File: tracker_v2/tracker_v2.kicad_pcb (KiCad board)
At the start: 2 copper layers, 69 x 51.6 mm, 26 parts, among them J1 USB_C_Receptacle_PowerOnly_6P, Q1 DMG9926UDM-7, U1 XIAO-ESP32-C6-SMD, U2 LIS3DH, U3 DW01A, U4 INA226AIDGSR, U5 TP4056-42-ESOP8

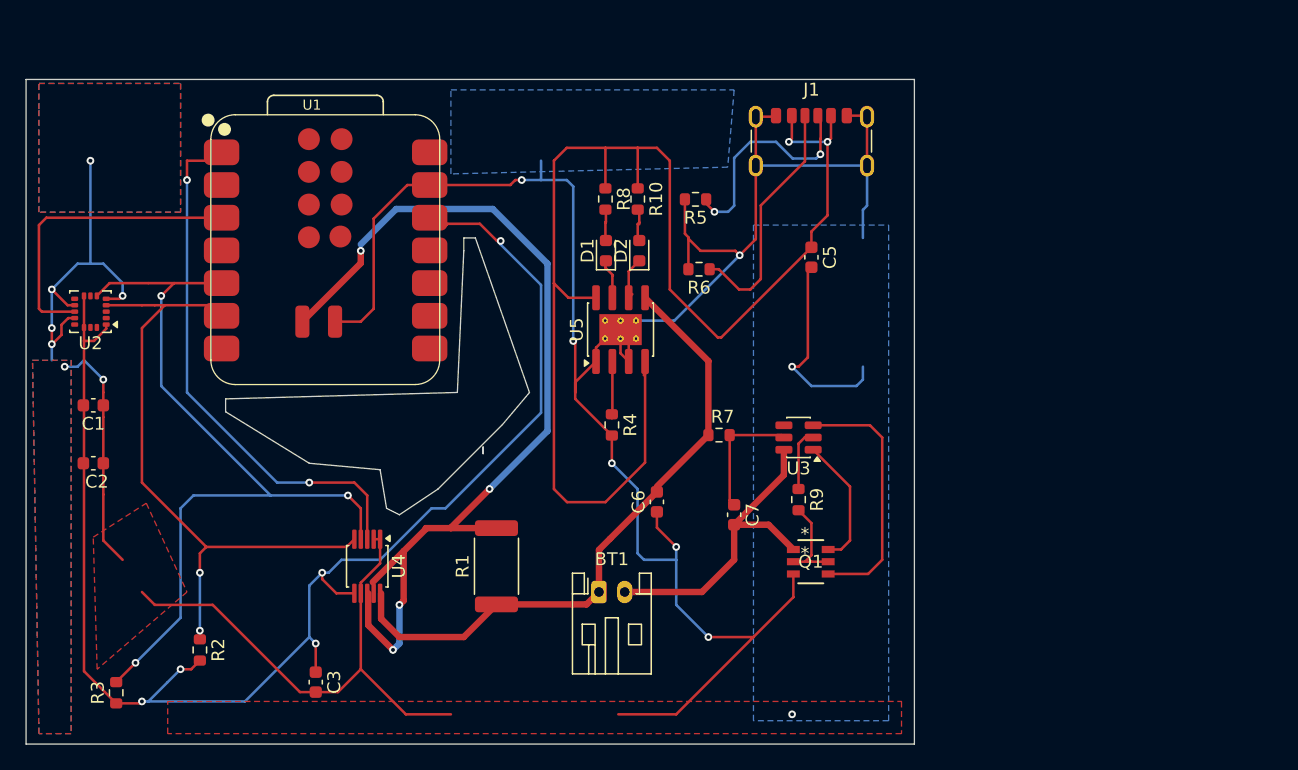
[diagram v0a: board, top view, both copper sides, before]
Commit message: started v2 , placement sure routing is being done
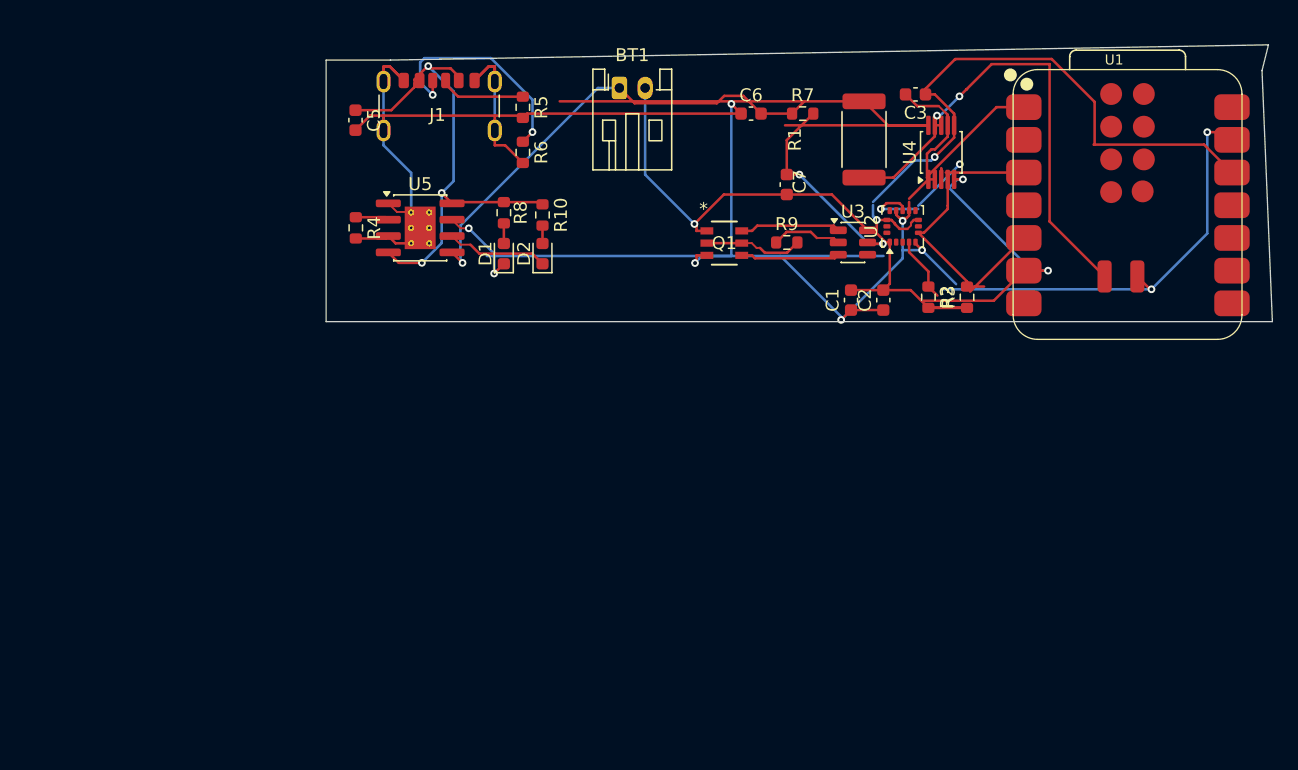
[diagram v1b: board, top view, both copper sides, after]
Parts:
- moved R3 72.9 mm to (170.1, 92.6)
- moved C3 65.2 mm to (166.1, 76.9), turned to 180 degrees
- moved U2 63.4 mm to (165.1, 87.1), turned to 90 degrees
- moved R2 62.9 mm to (167.1, 92.6)
- moved C2 62.7 mm to (163.6, 92.8), turned to 90 degrees
- moved U1 62.4 mm to (173.7, 96.0)
- moved C1 59.4 mm to (161.1, 92.8), turned to 90 degrees
- moved U4 55.0 mm to (168.1, 81.4), turned to 90 degrees
- moved R1 43.7 mm to (162.1, 80.4), turned to -90 degrees
- moved BT1 39.2 mm to (143.1, 76.4)
- moved C5 37.0 mm to (122.6, 78.9)
- moved C6 31.0 mm to (153.3, 78.3), turned to 0 degrees
- moved J1 29.0 mm to (129.1, 78.9)
- moved C7 26.0 mm to (156.1, 83.9)
- moved R7 25.8 mm to (157.3, 78.3)
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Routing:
- net GND: track 272.2 -> 201.3 mm, vias 15 -> 7
- net USB_VBUS: track 104.9 -> 39.2 mm, vias 2 -> 3
- net 3v3: track 112.7 -> 68.0 mm, vias 5 -> 2
- net SDA: track 63.3 -> 18.7 mm, vias 3 -> 0
- net /Shunt_Output: track 73.0 -> 37.7 mm, vias 4 -> 2
- net Net-(U1-D0): track 41.7 -> 10.6 mm, vias 2 -> 0
- net /Charging_and_Battery/BAT+: track 48.9 -> 77.5 mm, vias 0 -> 1
- net SCL: track 50.0 -> 28.1 mm
- net Net-(U3-OC): track 19.9 -> 7.71 mm
- net Net-(J1-CC2): track 17.7 -> 6.68 mm, vias 2 -> 0
- net Net-(U1-D2): track 23.8 -> 15.8 mm, vias 0 -> 2
- net Net-(U3-VCC): track 9.85 -> 16.5 mm, vias 0 -> 2
- net Net-(D2-K): track 3.67 -> 7.92 mm
- net /Charging_and_Battery/BAT-: track 25.1 -> 29.1 mm, vias 0 -> 1
- net Net-(D1-K): track 3.05 -> 6.97 mm, vias 0 -> 2
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- removed copper zone on B.Cu, net GND
- removed copper zone on F.Cu, net GND
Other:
- board size 69 x 51.6 mm -> 73.5 x 21.5 mm

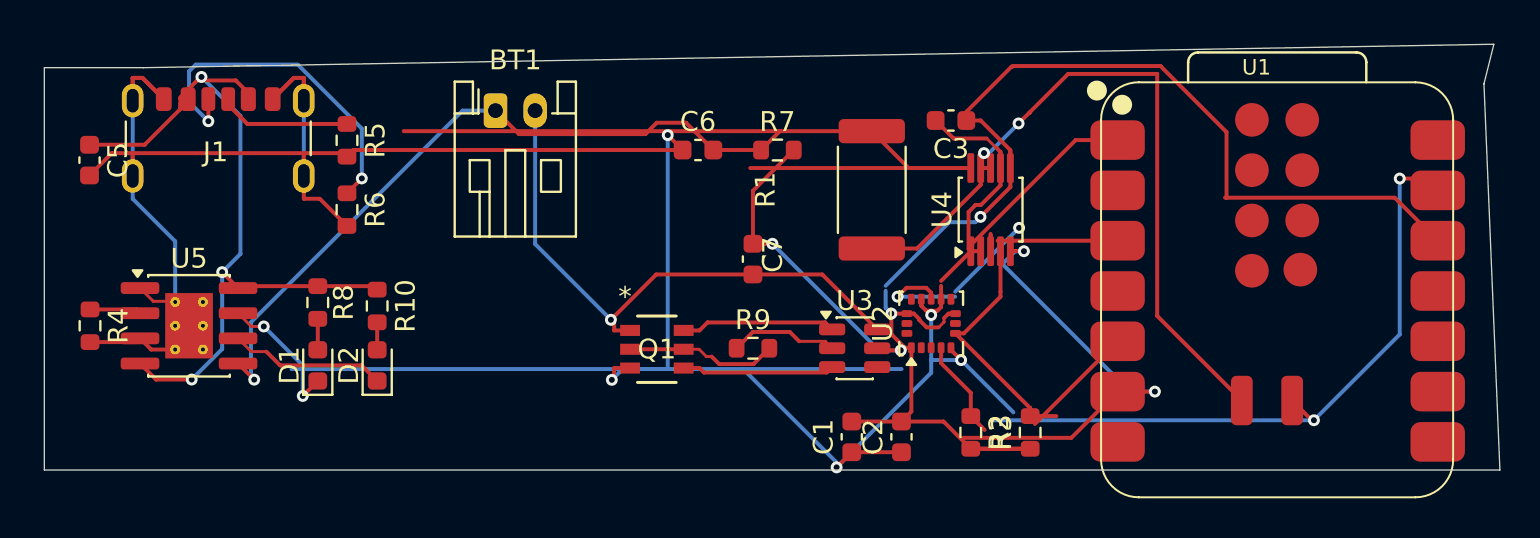
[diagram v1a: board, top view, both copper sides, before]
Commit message: added some connections
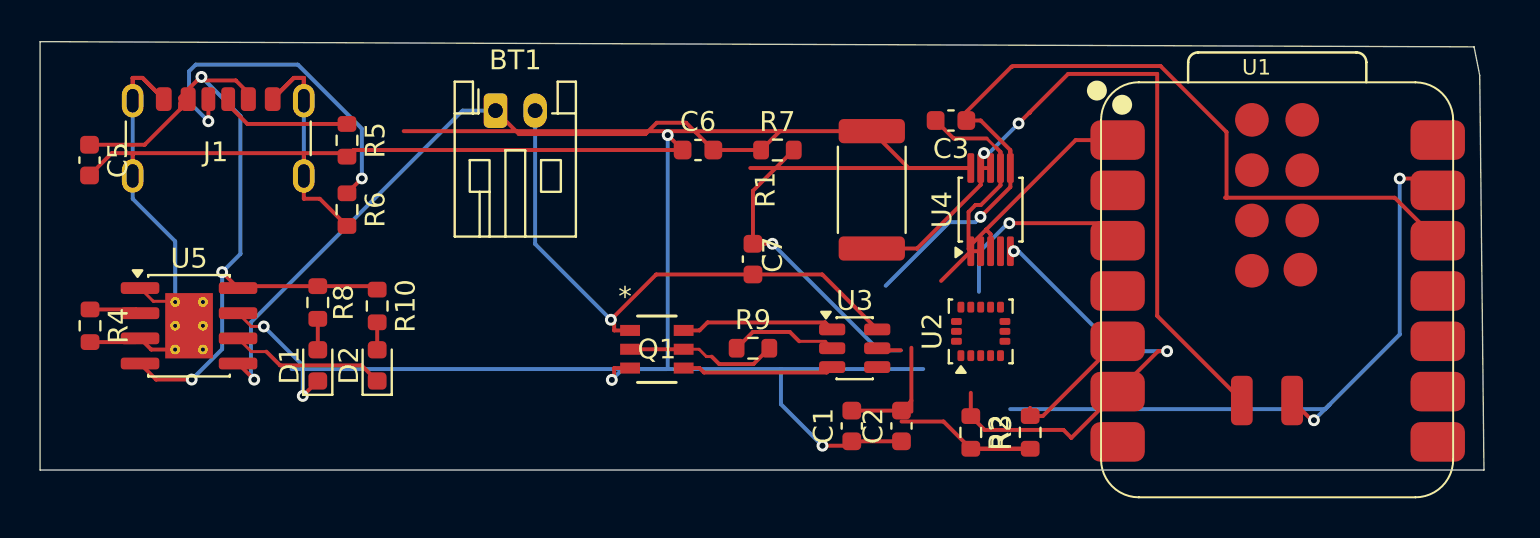
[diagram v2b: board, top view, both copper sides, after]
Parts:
- moved U2 2.53 mm to (167.6, 87.5)
- moved C1 0.55 mm to (161.1, 92.3)
- moved C2 0.55 mm to (163.6, 92.3)
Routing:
- net GND: track 201.3 -> 182.4 mm, vias 7 -> 5
- net SDA: track 18.7 -> 6.78 mm
- net 3v3: track 68.0 -> 60.4 mm, vias 2 -> 1
- net Net-(U1-D2): track 15.8 -> 10.0 mm, vias 2 -> 1
- net SCL: track 28.1 -> 23.2 mm
- net Net-(U3-VCC): vias 2 -> 1
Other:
- board size 73.5 x 21.5 mm -> 72.9 x 21.6 mm

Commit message: completed v2 routing
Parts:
- added TP1: TestPoint, TestPoint:TestPoint_Pad_D1.0mm, F.Cu at (124.5, 92.0)
- added TP2: TestPoint, TestPoint:TestPoint_Pad_D1.0mm, F.Cu at (145.5, 92.5)
- added TP3: TestPoint, TestPoint:TestPoint_Pad_D1.0mm, F.Cu at (171.0, 87.5)
- added TP4: TestPoint, TestPoint:TestPoint_Pad_D1.0mm, F.Cu at (171.5, 85.0)
- added TP5: TestPoint, TestPoint:TestPoint_Pad_D1.0mm, F.Cu at (171.5, 82.0)
- added TP6: TestPoint, TestPoint:TestPoint_Pad_D1.0mm, F.Cu at (170.0, 74.0)
- added TP7: TestPoint, TestPoint:TestPoint_Pad_D1.0mm, F.Cu at (125.0, 74.5)
- added TP8: TestPoint, TestPoint:TestPoint_Pad_D1.0mm, F.Cu at (151.0, 75.5)
- moved J1 2.90 mm to (131.8, 77.8)
- moved R5 2.90 mm to (138.3, 76.8)
- moved R6 2.90 mm to (138.3, 80.3)
- moved R4 2.90 mm to (125.3, 86.2)
- moved C5 2.90 mm to (125.3, 77.8)
- moved U5 2.90 mm to (130.3, 86.2)
- moved D1 2.90 mm to (136.8, 88.2)
- moved D2 2.90 mm to (139.8, 88.2)
- moved R10 2.90 mm to (139.8, 85.2)
- moved R8 2.90 mm to (136.8, 85.0)
- moved R2 0.43 mm to (167.1, 92.2)
- moved R3 0.43 mm to (170.1, 92.2)
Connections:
- U2 pad 7: unconnected-(U2-SDO-Pad7) -> 3v3
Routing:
- net GND: track 182.4 -> 246.9 mm, vias 5 -> 12
- net /Charging_and_Battery/BAT+: track 77.5 -> 45.9 mm, vias 1 -> 2
- net USB_VBUS: track 39.2 -> 51.0 mm
- net 3v3: track 60.4 -> 70.7 mm, vias 1 -> 2
- net SDA: track 6.78 -> 16.2 mm
- net (no net): track 0.00 -> 2.11 mm, vias 0 -> 3
- net Net-(U1-D0): track 10.9 -> 9.51 mm
- net Net-(U3-VCC): track 16.5 -> 15.2 mm, vias 1 -> 2
- net SCL: track 23.2 -> 24.3 mm
- net /Shunt_Output: track 37.7 -> 38.7 mm
- net Net-(U1-D2): track 10.0 -> 10.8 mm, vias 1 -> 2
- net /Charging_and_Battery/BAT-: track 29.1 -> 29.3 mm, vias 1 -> 2
- added copper zone on B.Cu, net GND
- added copper zone on F.Cu, net GND
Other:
- board size 72.9 x 21.6 mm -> 71 x 22.1 mm
- board text added: "+"
- board text added: "-"

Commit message: removed a GND trace under the chip and connected it to a common ground
like the title says
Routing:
- net GND: track 246.9 -> 235.6 mm
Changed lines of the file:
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@@
 	)
 	(segment
-		(start 180.5 88.5)
-		(end 184 88.5)
+		(start 188.747 79.7814)
+		(end 188.5284 80)
 		(width 0.2)
 		(layer "B.Cu")
@@
 	)
 	(segment
-		(start 186.25 86.25)
-		(end 188.747 83.753)
+		(start 183 88.5)
+		(end 183 87)
+		(width 0.2)
+		(layer "B.Cu")
+		(net "GND")
+	)
+	(segment
+		(start 188.5284 80)
+		(end 187.5 80)
 		(width 0.2)
 		(layer "B.Cu")
@@
 		(start 173 90)
 		(end 173.9 89.1)
-		(width 0.2)
-		(layer "B.Cu")
-		(net "GND")
-	)
-	(segment
-		(start 188.747 83.753)
-		(end 188.747 79.7814)
 		(width 0.2)
 		(layer "B.Cu")
@@
 		(width 0.2)
 		(layer "B.Cu")
-		(net "GND")
-	)
-	(segment
-		(start 184 88.5)
-		(end 186.25 86.25)
-		(width 0.2)
-		(layer "B.Cu")
